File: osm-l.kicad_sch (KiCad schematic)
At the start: 48 parts, among them SW1 SW_KMR211NGLFS_SMD, U14 OSM-L_Carrier-side, U39 74AUP2G132, U40 74AUP2G132

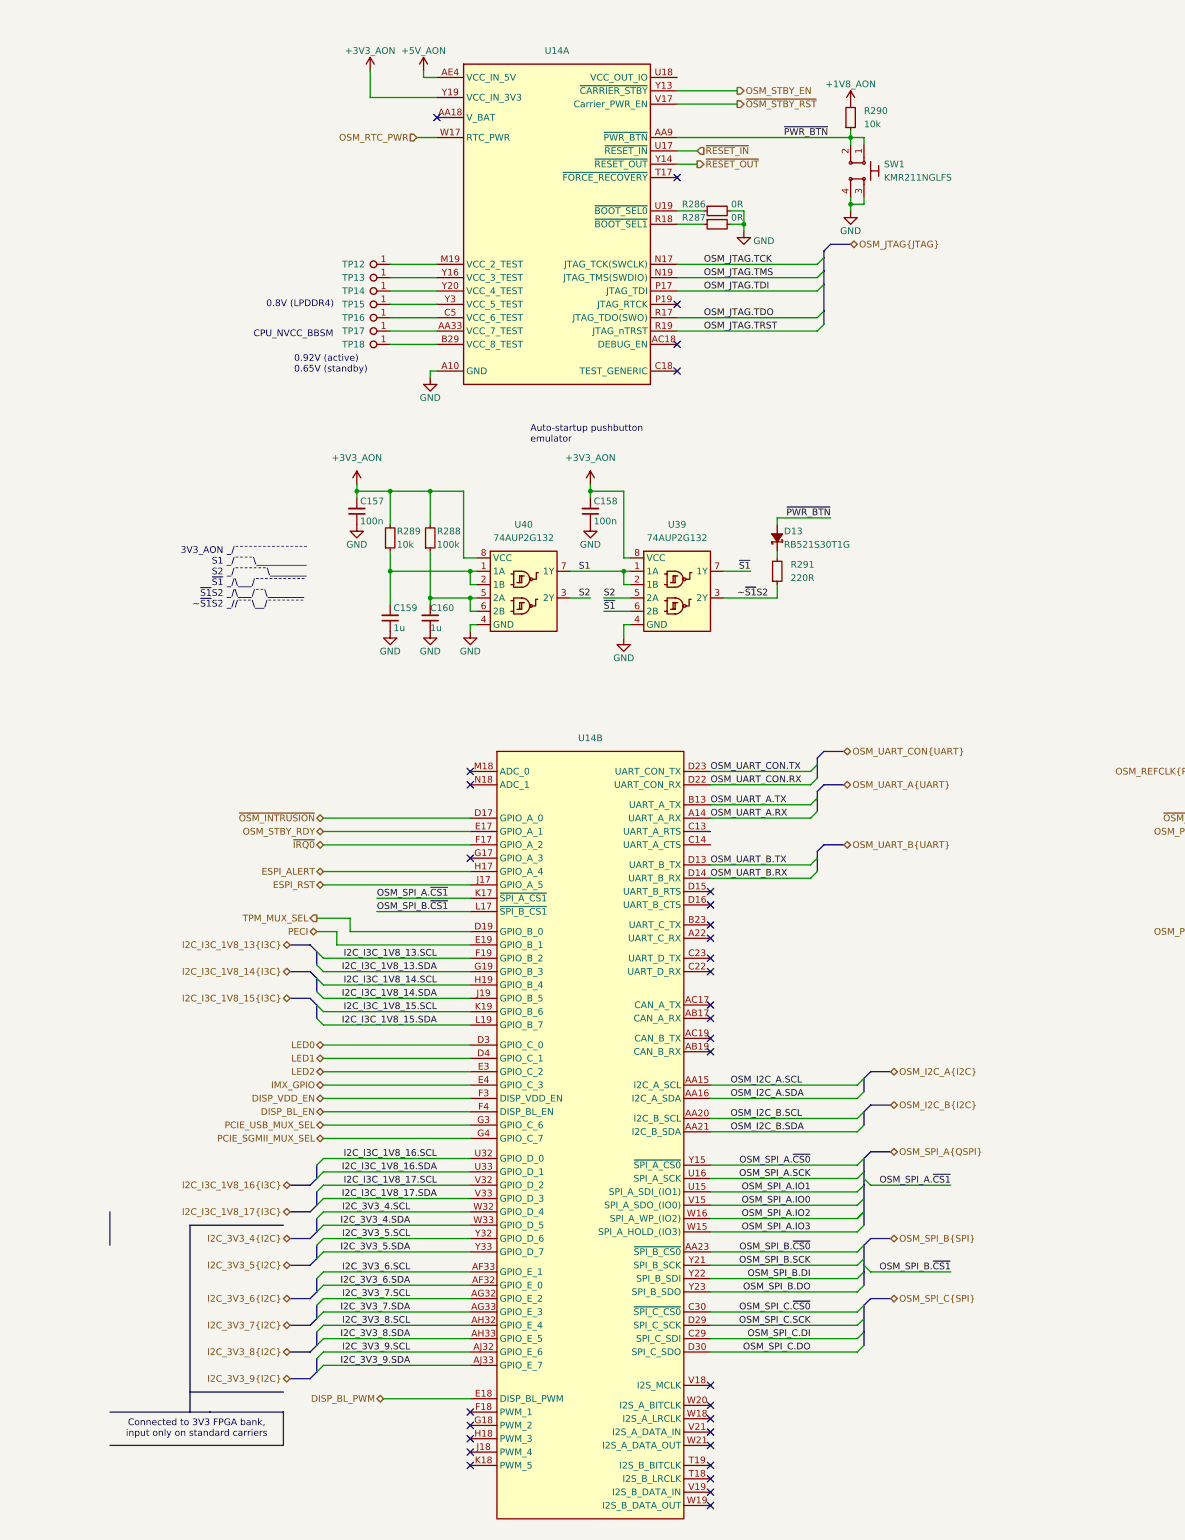
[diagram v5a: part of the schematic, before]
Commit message: [#83609] Connect all OSM signals
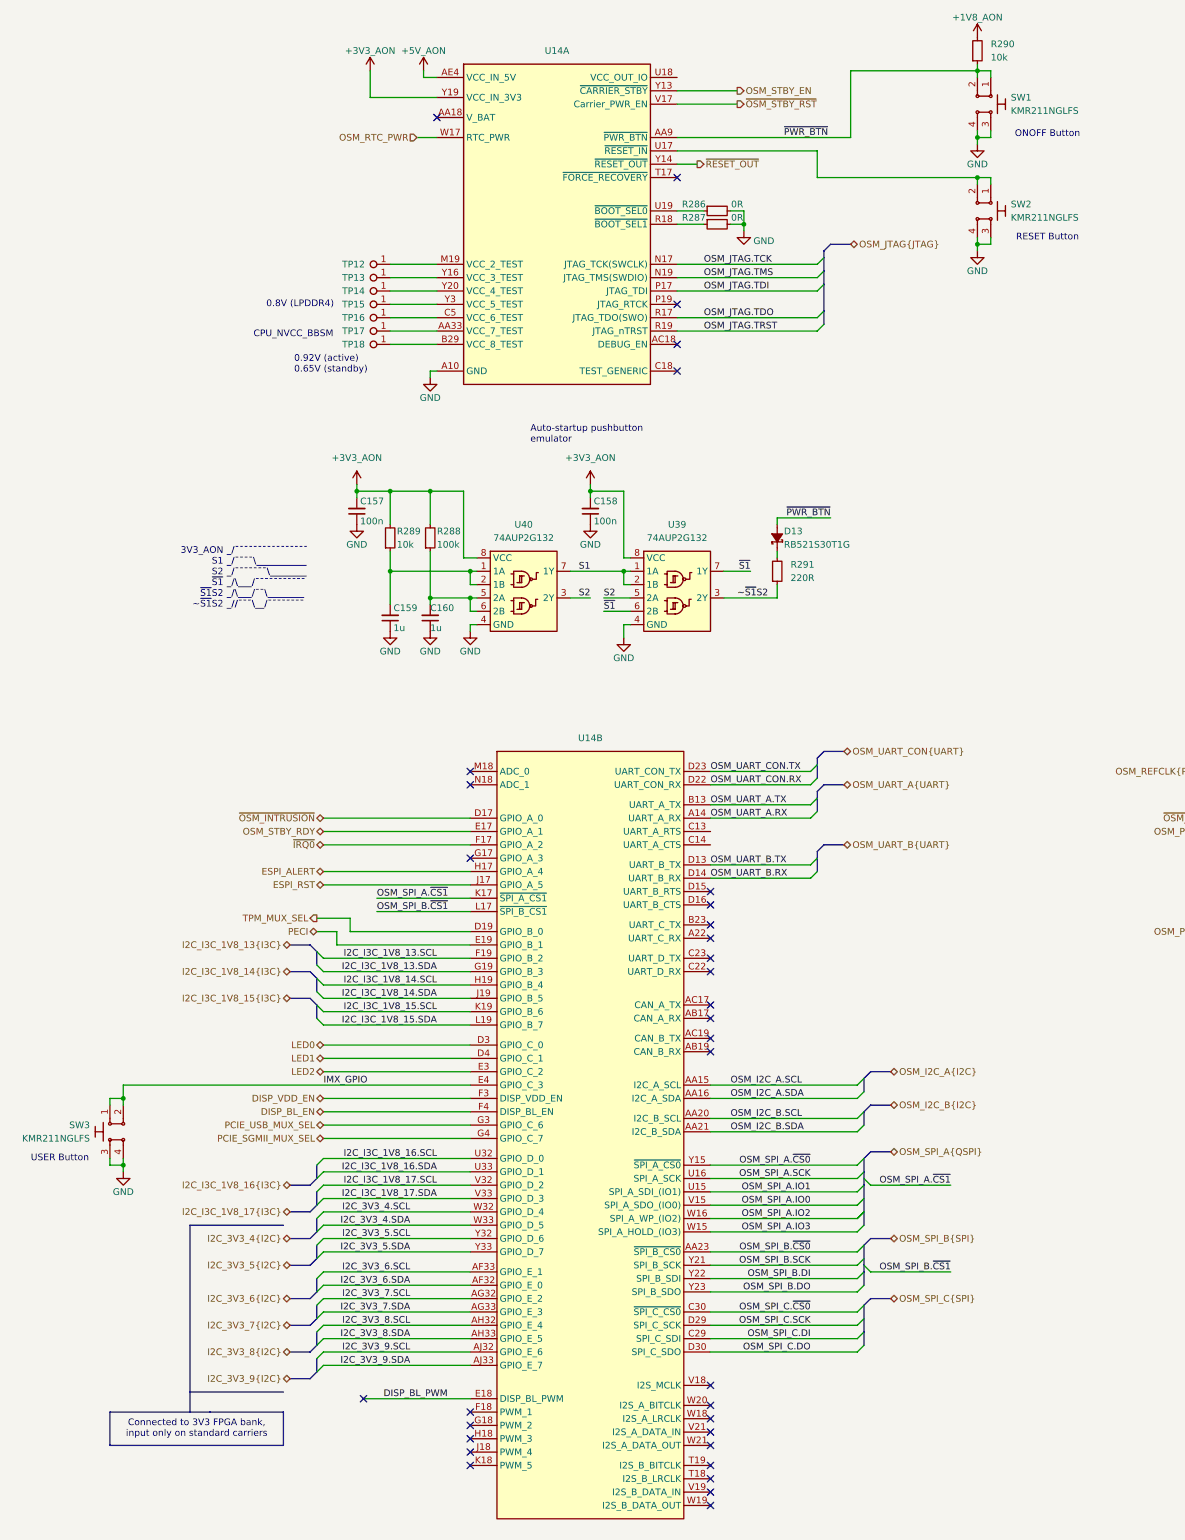
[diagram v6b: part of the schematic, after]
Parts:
- added SW2, SW3: SW_KMR211NGLFS_SMD, antmicro-footprints:SW_KMR211NGLFS_SMD, symbol antmicroPushbuttonSwitches:SW_KMR211NGLFS_SMD
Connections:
- net GND: now also SW2.3, SW2.4, SW3.3, SW3.4
- net IMX_GPIO: now also SW3.1, SW3.2
- net ~{RESET_IN}: no longer names the net of U14.U17 (~{RESET_IN})
- net ~{RESET_IN}: now also SW2.1, SW2.2
- no-connect marks 329 -> 330
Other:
- note added: "ONOFF Button"
- note added: "RESET Button"
- note added: "USER Button"
- moved on the sheet: R290, SW1

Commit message: [#83609] Reannotate board
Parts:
- renumbered C157 to C1, C138 to C10, C159 to C2, C160 to C3, C158 to C4, C136 to C5, C134 to C6, C137 to C7, C135 to C8, C139 to C9, D13 to D1, R289 to R55, R288 to R56, R286 to R57, R287 to R58, R291 to R59, R290 to R60, R187 to R61, R188 to R62, R185 to R63, R186 to R64, R224 to R65, R225 to R66, R226 to R67, R227 to R68, R228 to R69, R229 to R70, R230 to R71, R231 to R72, R195 to R73, R196 to R74, R189 to R75, R190 to R76, R193 to R77, R194 to R78, R191 to R79, R192 to R80, SW3 to SW1, SW1 to SW2, SW2 to SW3, TP12 to TP1, TP13 to TP2, TP14 to TP3, TP15 to TP4, TP16 to TP5, TP17 to TP6, TP18 to TP7, U14 to U1, U40 to U2, U39 to U3

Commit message: [#83736] WIP: Clear ERC
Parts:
- added TP30: TP_0.75mm_SMD, antmicro-footprints:TP_SMD_0.75mm, symbol antmicroTestPoints:TP_0.75mm_SMD
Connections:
- net at U1.U18 (VCC_OUT_IO): now also TP30.1
- no-connect marks 330 -> 332
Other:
- moved on the sheet: R60
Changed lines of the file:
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@@
 	)
 	(junction
+		(at 201.93 27.94)
+		(diameter 0)
+		(color 0 0 0 0)
+	)
+	(junction
 		(at 95.25 107.95)
 		(diameter 0)
@@
 	)
 	(no_connect
+		(at 148.59 172.72)
+	)
+	(no_connect
 		(at 534.67 142.24)
 	)
@@
 	)
 	(no_connect
+		(at 148.59 175.26)
+	)
+	(no_connect
 		(at 439.42 252.73)
 	)
@@
 	(wire
 		(pts
-			(xy 168.91 77.47) (xy 142.24 77.47)
-		)
-		(stroke
-			(width 0)
-			(type default)
-		)
-	)
-	(wire
-		(pts
 			(xy 81.28 107.95) (xy 81.28 109.22)
 		)
@@
 		)
 	)
+	(wire
+		(pts
+			(xy 142.24 77.47) (xy 168.91 77.47)
+		)
+		(stroke
+			(width 0)
+			(type default)
+		)
+	)
 	(bus
 		(pts
@@
 	(wire
 		(pts
-			(xy 199.39 27.94) (xy 201.93 27.94)
-		)
-		(stroke
-			(width 0)
-			(type default)
-		)
-	)
-	(wire
-		(pts
 			(xy 87.63 397.51) (xy 102.87 397.51)
 		)
@@
 	(wire
 		(pts
+			(xy 201.93 27.94) (xy 199.39 27.94)
+		)
+		(stroke
+			(width 0)
+			(type default)
+		)
+	)
+	(wire
+		(pts
 			(xy 148.59 229.87) (xy 176.53 229.87)
 		)
@@
 	(wire
 		(pts
+			(xy 144.78 29.21) (xy 142.24 29.21)
+		)
+		(stroke
+			(width 0)
+			(type default)
+		)
+	)
+	(wire
+		(pts
 			(xy 148.59 243.84) (xy 176.53 243.84)
 		)
@@
 		)
 	)
+	(wire
+		(pts
+			(xy 201.93 20.32) (xy 201.93 21.59)
+		)
+		(stroke
+			(width 0)
+			(type default)
+		)
+	)
 	(bus
 		(pts
@@
 	(wire
 		(pts
-			(xy 199.39 26.67) (xy 199.39 27.94)
+			(xy 201.93 26.67) (xy 201.93 27.94)
 		)
 		(stroke
@@
 	(symbol
 		(lib_id "antmicropower:+1V8_AON")
-		(at 199.39 21.59 0)
+		(at 201.93 20.32 0)
 		(unit 1)
 		(exclude_from_sim no)
@@
 		(dnp no)
 		(property "Reference" "#PWR016"
-			(at 214.63 24.13 0)
+			(at 217.17 22.86 0)
 			(effects
 				(font
@@
 		)
 		(property "Value" "+1V8_AON"
-			(at 199.39 17.78 0)
+			(at 201.93 16.51 0)
 			(effects
 				(font
@@
 		)
 		(property "Footprint" ""
-			(at 214.63 29.21 0)
+			(at 217.17 27.94 0)
 			(effects
 				(font
@@
 		)
 		(property "Datasheet" ""
-			(at 214.63 31.75 0)
+			(at 217.17 30.48 0)
 			(effects
 				(font
@@
 		)
 		(property "Description" ""
-			(at 199.39 21.59 0)
+			(at 201.93 20.32 0)
 			(effects
 				(font
@@
 		)
 		(property "Author" "Antmicro"
-			(at 214.63 26.67 0)
+			(at 217.17 25.4 0)
 			(effects
 				(font
@@
 		)
 		(property "License" "Apache-2.0"
-			(at 214.63 29.21 0)
+			(at 217.17 27.94 0)
 			(effects
 				(font
@@
 	)
 	(symbol
+		(lib_id "antmicroTestPoints:TP_0.75mm_SMD")
+		(at 144.78 29.21 0)
+		(unit 1)
+		(exclude_from_sim no)
+		(in_bom no)
+		(on_board yes)
+		(dnp no)
+		(property "Reference" "TP30"
+			(at 149.098 29.21 0)
+			(effects
+				(font
+					(size 1.27 1.27)
+					(thickness 0.15)
+				)
+				(justify left)
+			)
+		)
+		(property "Value" "TP_0.75mm_SMD"
+			(at 154.94 33.02 0)
+			(effects
+				(font
+					(size 1.27 1.27)
+					(thickness 0.15)
+				)
+				(justify left bottom)
+				(hide yes)
+			)
+		)
+		(property "Footprint" "antmicro-footprints:TP_SMD_0.75mm"
+			(at 154.94 35.56 0)
+			(effects
+				(font
+					(size 1.27 1.27)
+					(thickness 0.15)
+				)
+				(justify left bottom)
+				(hide yes)
+			)
+		)
+		(property "Datasheet" ""
+			(at 162.56 41.91 0)
+			(effects
+				(font
+					(size 1.27 1.27)
+					(thickness 0.15)
+				)
+				(justify left bottom)
+				(hide yes)
+			)
+		)
+		(property "Description" "SMT test point"
+			(at 144.78 29.21 0)
+			(effects
+				(font
+					(size 1.27 1.27)
+				)
+				(hide yes)
+			)
+		)
+		(property "MPN" ""
+			(at 155.575 40.64 0)
+			(effects
+				(font
+					(size 1.27 1.27)
+					(thickness 0.15)
+				)
+				(justify left bottom)
+				(hide yes)
+			)
+		)
+		(property "Manufacturer" ""
+			(at 155.575 35.56 0)
+			(effects
+				(font
+					(size 1.27 1.27)
+					(thickness 0.15)
+				)
+				(justify left bottom)
+				(hide yes)
+			)
+		)
+		(property "Author" "Antmicro"
+			(at 154.94 38.1 0)
+			(effects
+				(font
+					(size 1.27 1.27)
+					(thickness 0.15)
+				)
+				(justify left bottom)
+				(hide yes)
+			)
+		)
+		(property "License" "Apache-2.0"
+			(at 154.94 40.64 0)
+			(effects
+				(font
+					(size 1.27 1.27)
+					(thickness 0.15)
+				)
+				(justify left bottom)
+				(hide yes)
+			)
+		)
+		(pin "1"
+		)
+		(instances
+			(project ""
+				(path "/5f636c45-3c15-4731-8931-4625e0dab7e4/626fa623-3c57-4093-88cf-23d76305ad93"
+					(reference "TP30")
+					(unit 1)
+				)
+			)
+		)
+	)
+	(symbol
 		(lib_id "antmicroCapacitors0402:C_220n_0402")
 		(at 285.75 195.58 0)
@@
 	(symbol
 		(lib_id "antmicroResistors0402:R_10k_0402")
-		(at 199.39 26.67 90)
+		(at 201.93 26.67 90)
 		(unit 1)
 		(exclude_from_sim no)
@@
 		(fields_autoplaced yes)
 		(property "Reference" "R60"
-			(at 201.93 22.86 90)
+			(at 204.47 22.86 90)
 			(effects
 				(font
@@
 		)
 		(property "Value" "R_10k_0402"
-			(at 212.09 6.35 0)
+			(at 214.63 6.35 0)
 			(effects
 				(font
@@
 		)
 		(property "Footprint" "antmicro-footprints:R_0402_1005Metric"
-			(at 214.63 6.35 0)
+			(at 217.17 6.35 0)
 			(effects
 				(font
@@
 		)
 		(property "Datasheet" "https://www.bourns.com/docs/product-datasheets/cr.pdf"
-			(at 217.17 6.35 0)
+			(at 219.71 6.35 0)
 			(effects
 				(font
@@
 		)
 		(property "Description" "SMD Chip Resistor, 10 kohm, ± 1%, 62.5 mW, 0402 [1005 Metric], Thick Film, General Purpose"
-			(at 199.39 26.67 0)
+			(at 201.93 26.67 0)
 			(effects
 				(font
@@
 		)
 		(property "MPN" "CR0402-FX-1002GLF"
-			(at 219.71 6.35 0)
+			(at 222.25 6.35 0)
 			(effects
 				(font
@@
 		)
 		(property "Manufacturer" "Bourns"
-			(at 222.25 6.35 0)
+			(at 224.79 6.35 0)
 			(effects
 				(font
@@
 		)
 		(property "License" "Apache-2.0"
-			(at 224.79 6.35 0)
+			(at 227.33 6.35 0)
 			(effects
 				(font
@@
 		)
 		(property "Author" "Antmicro"
-			(at 227.33 6.35 0)
+			(at 229.87 6.35 0)
 			(effects
 				(font
@@
 		)
 		(property "Val" "10k"
-			(at 201.93 25.4 90)
+			(at 204.47 25.4 90)
 			(effects
 				(font
@@
 		)
 		(property "Tolerance" "1%"
-			(at 209.55 6.35 0)
+			(at 212.09 6.35 0)
 			(effects
 				(font
